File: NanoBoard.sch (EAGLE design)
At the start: 16 parts, among them IC1 ATMEGA32U2-TQFP, Q1 16MHz

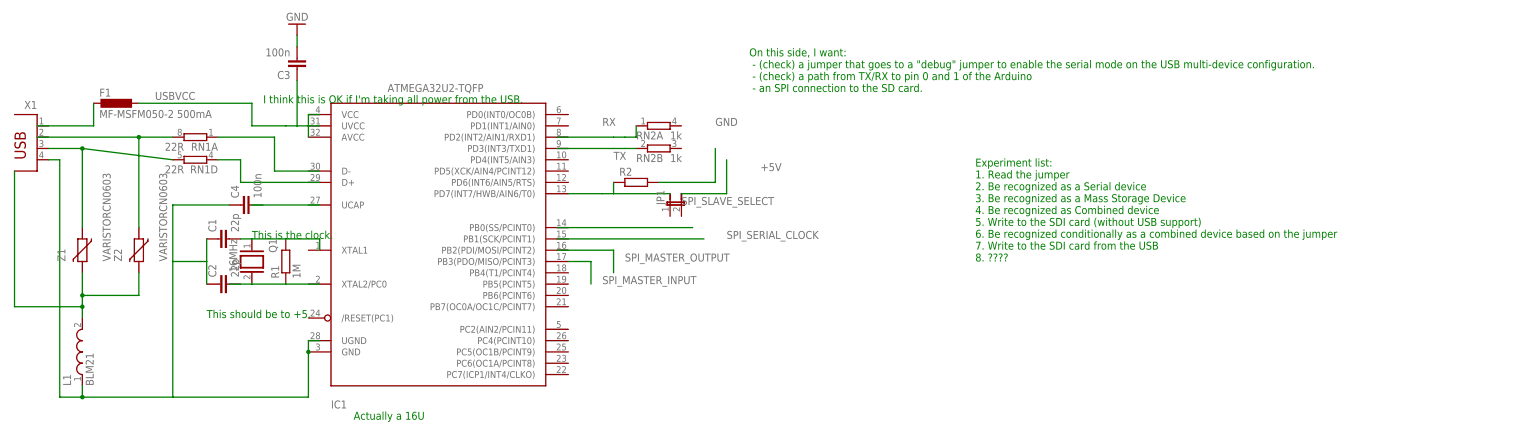
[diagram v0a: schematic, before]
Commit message: Fixed some errors Eagle discovered, and changed the pins the LED is on because they are analog pins.
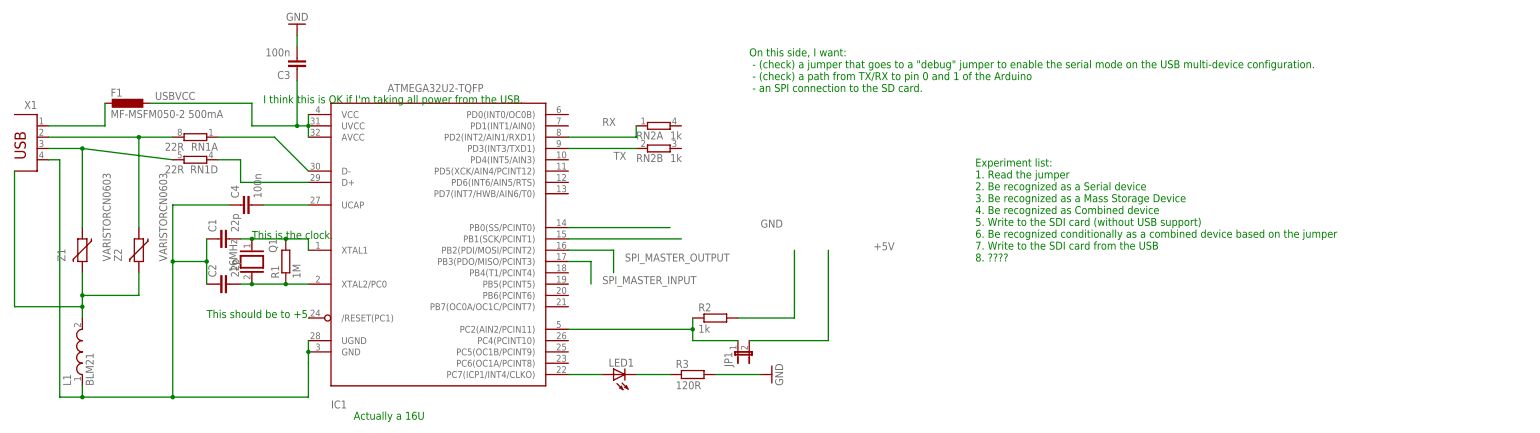
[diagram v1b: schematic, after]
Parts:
- added LED1: (no value), adafruit:LED
- added R3: 120R, resistor:R-EU_0204/2V
- R2: value (none) -> 1k
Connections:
- new net +5V: JP1.2
- new net N$12: IC1.PB1(SCK/PCINT1)
- new net N$13: IC1.PB0(SS/PCINT0)
- new net N$14: IC1.PC7(ICP1/INT4/CLKO), LED1.A
- new net N$15: LED1.C, R3.1
- new net N$5: C4.2, IC1.UCAP
- new net SPI_MASTER_OUTPUT: IC1.PB2(PDI/MOSI/PCINT2)
- net GND: now also R3.2
- net N$1: now also X1.1
- net N$10: now also IC1.UGND
- net N$11: now also IC1.PC2(AIN2/PCIN11), JP1.1; no longer IC1.PD7(INT7/HWB/AIN6/T0)
- net N$2: now also X1.2
- net N$6: now also IC1.D-
- net N$7: now also IC1.D+
- net N$8: now also IC1.XTAL1
- net N$9: now also C2.2, IC1.XTAL2/PC0
- net RX: now also IC1.PD2(INT2/AIN1/RXD1)
- net TX: now also IC1.PD3(INT3/TXD1)
- net USBVCC: now also IC1.VCC
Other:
- moved on the sheet: F1, JP1, R2
